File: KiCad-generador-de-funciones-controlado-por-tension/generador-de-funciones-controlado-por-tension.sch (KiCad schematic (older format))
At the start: 51 parts

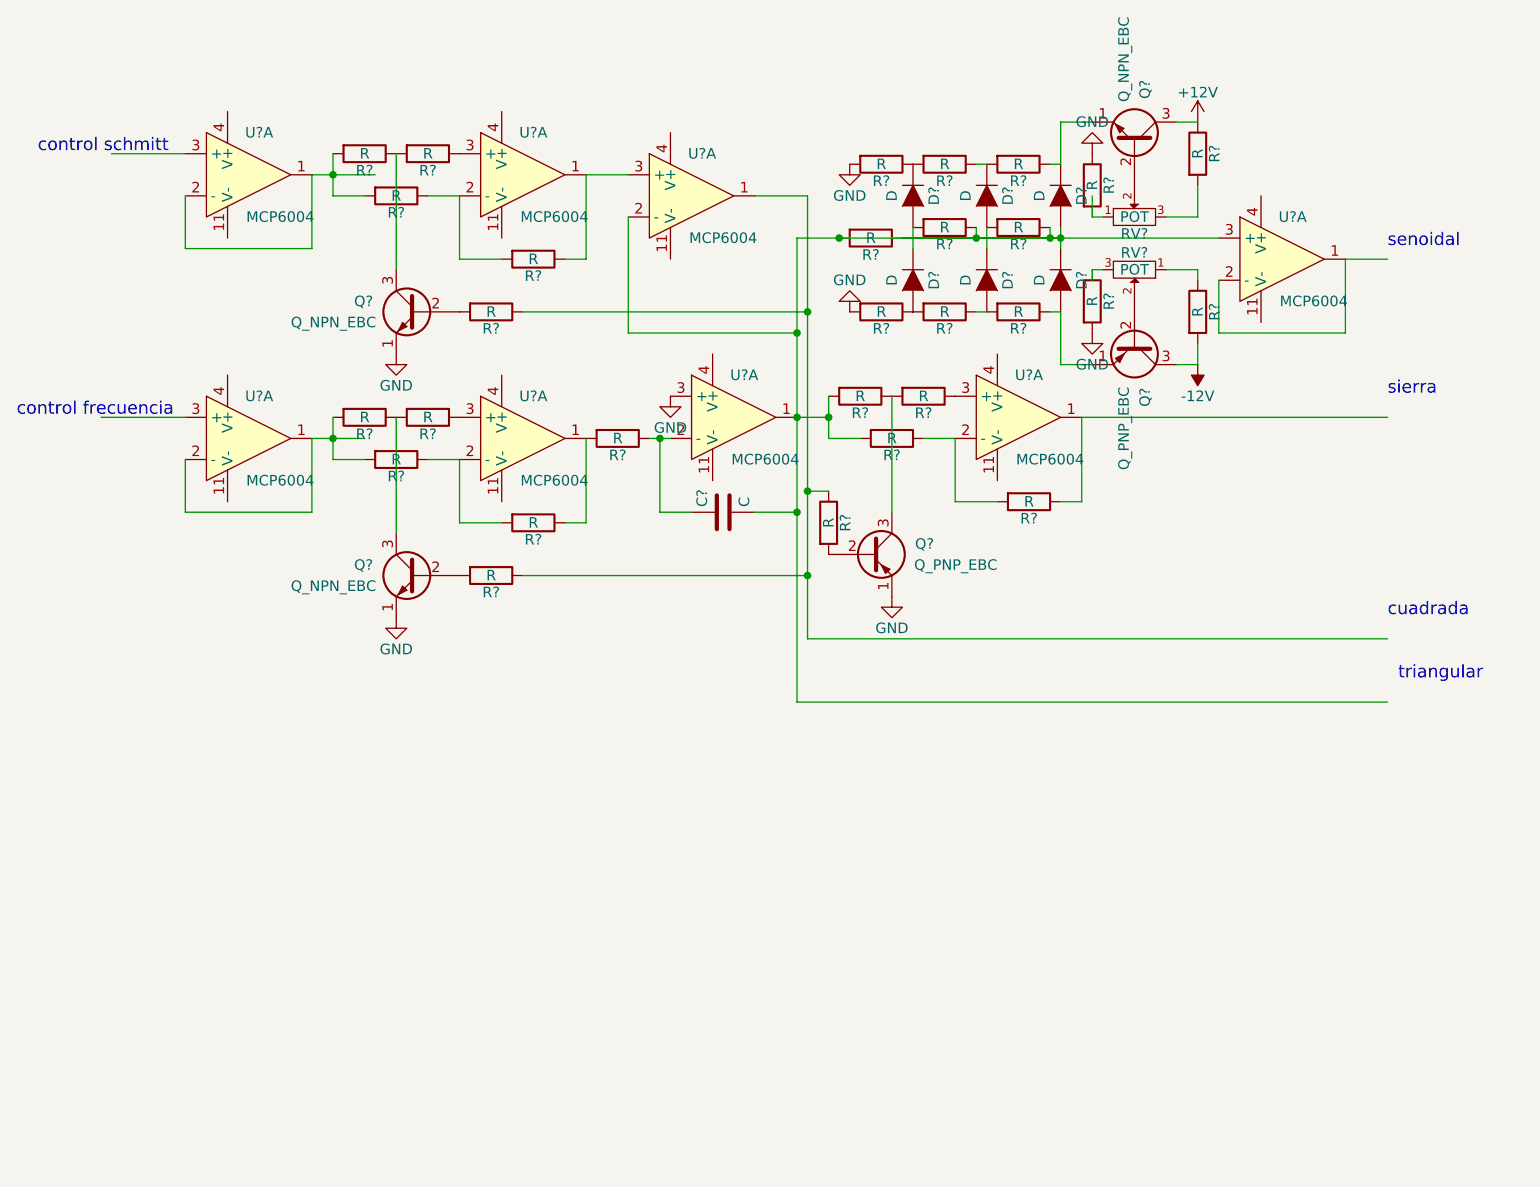
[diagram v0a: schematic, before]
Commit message: plano en pdf de la parte de KiCad
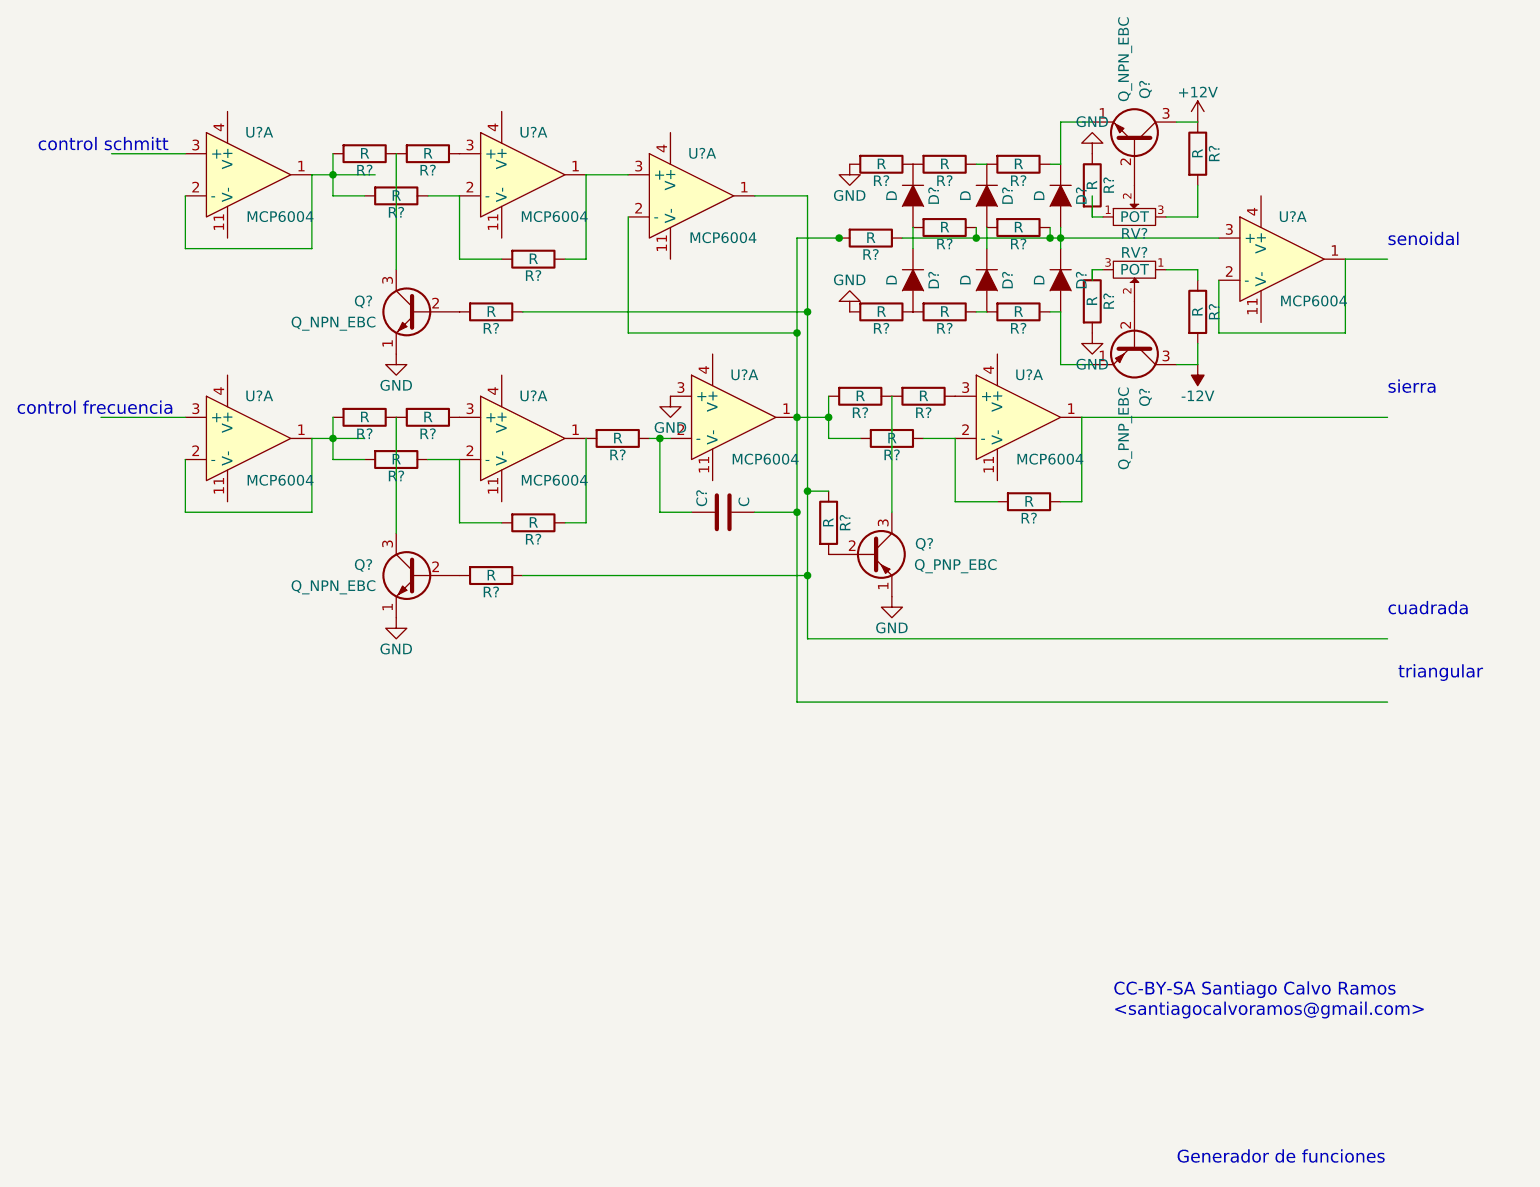
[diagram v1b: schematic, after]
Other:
- note added: "CC-BY-SA Santiago Calvo Ramos\n<santiagocalvoramos@gmail.com>"
- note added: "Generador de funciones"
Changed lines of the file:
@@
 Wire Wire Line
 	8150 3550 8150 3200
-Wire Wire Line
-	5550 3100 6800 3100
 Connection ~ 5750 3100
 Connection ~ 5550 3550
@@
 Wire Wire Line
 	2650 3950 2250 3950
+Text Notes 7050 6800 0    60   ~ 0
+CC-BY-SA Santiago Calvo Ramos\n<santiagocalvoramos@gmail.com>
+Text Notes 7350 7500 0    60   ~ 0
+Generador de funciones
+Wire Wire Line
+	5750 3100 5550 3100
 $EndSCHEMATC

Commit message: modificado esquema en KiCad
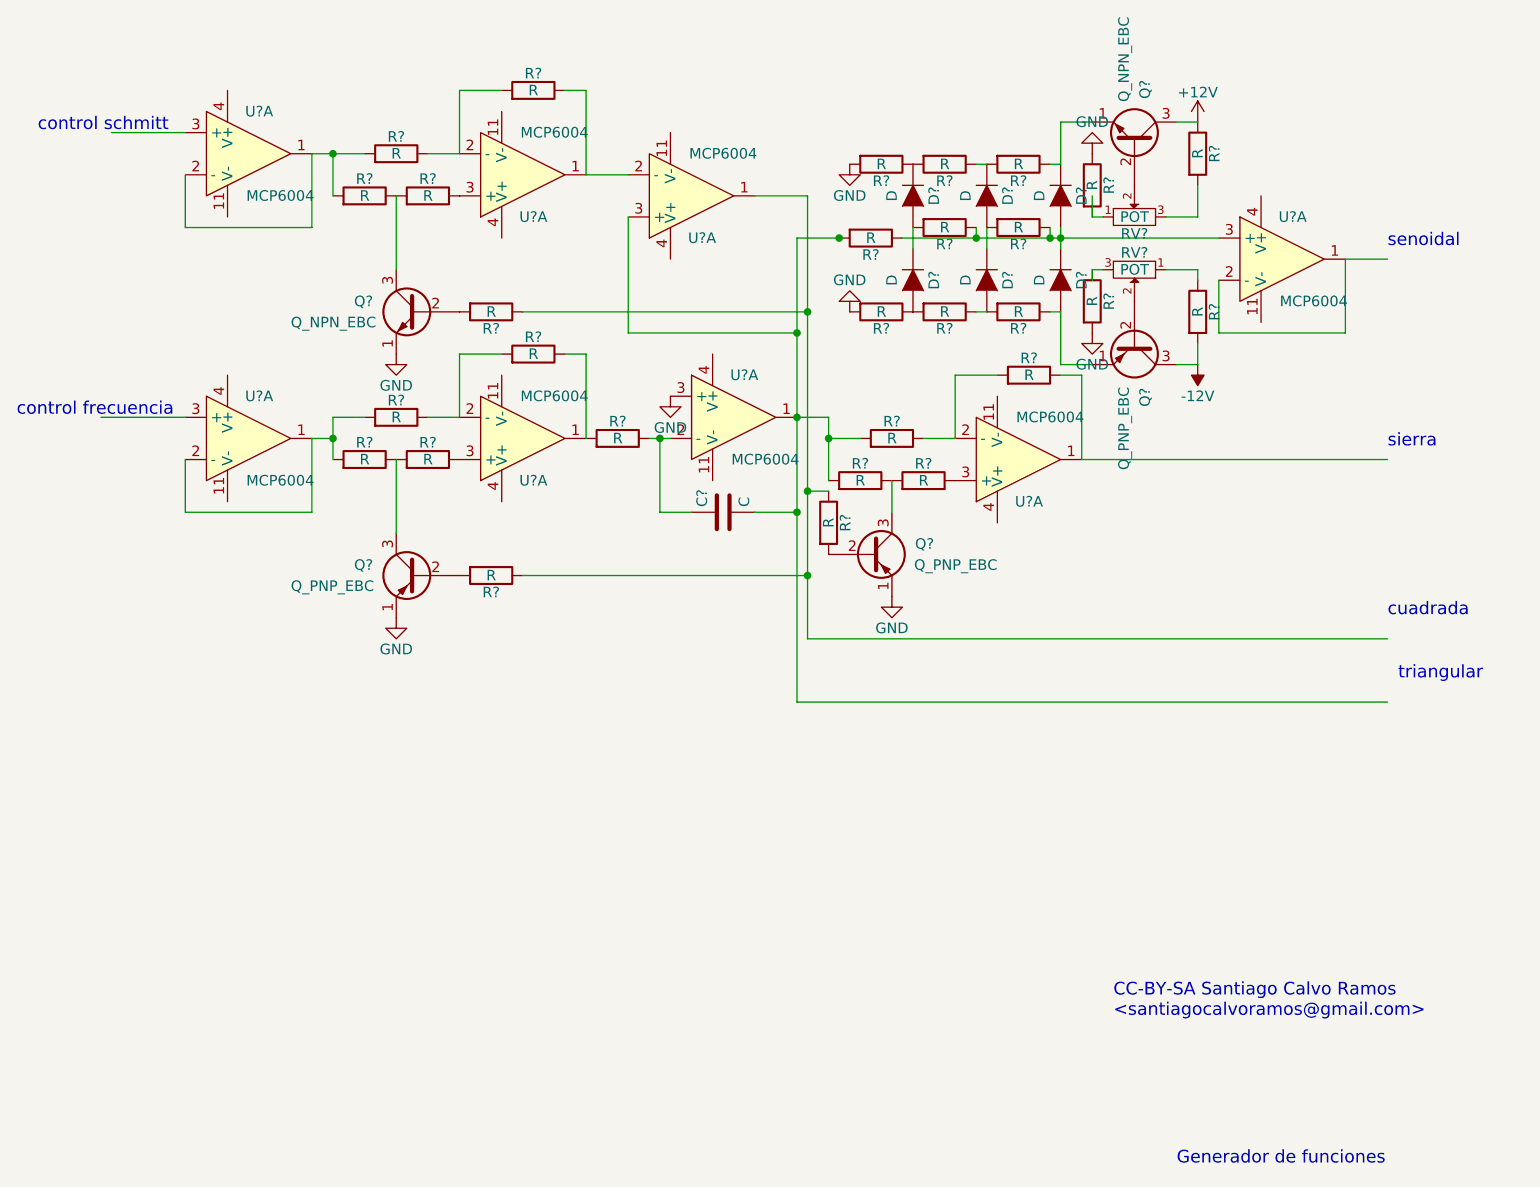
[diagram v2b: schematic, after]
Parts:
- removed Q? (x2): Q_NPN_EBC, symbol Q_NPN_EBC
- added Q?: Q_NPN_EBC, symbol Q_NPN_EBC
- added Q?: Q_PNP_EBC, symbol Q_PNP_EBC
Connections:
- wire segments 81 -> 80
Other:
- moved on the sheet: R?, U?A
